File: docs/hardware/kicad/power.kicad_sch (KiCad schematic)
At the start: 18 parts, among them K1 125 A 24 V, Q1 IRLZ44N

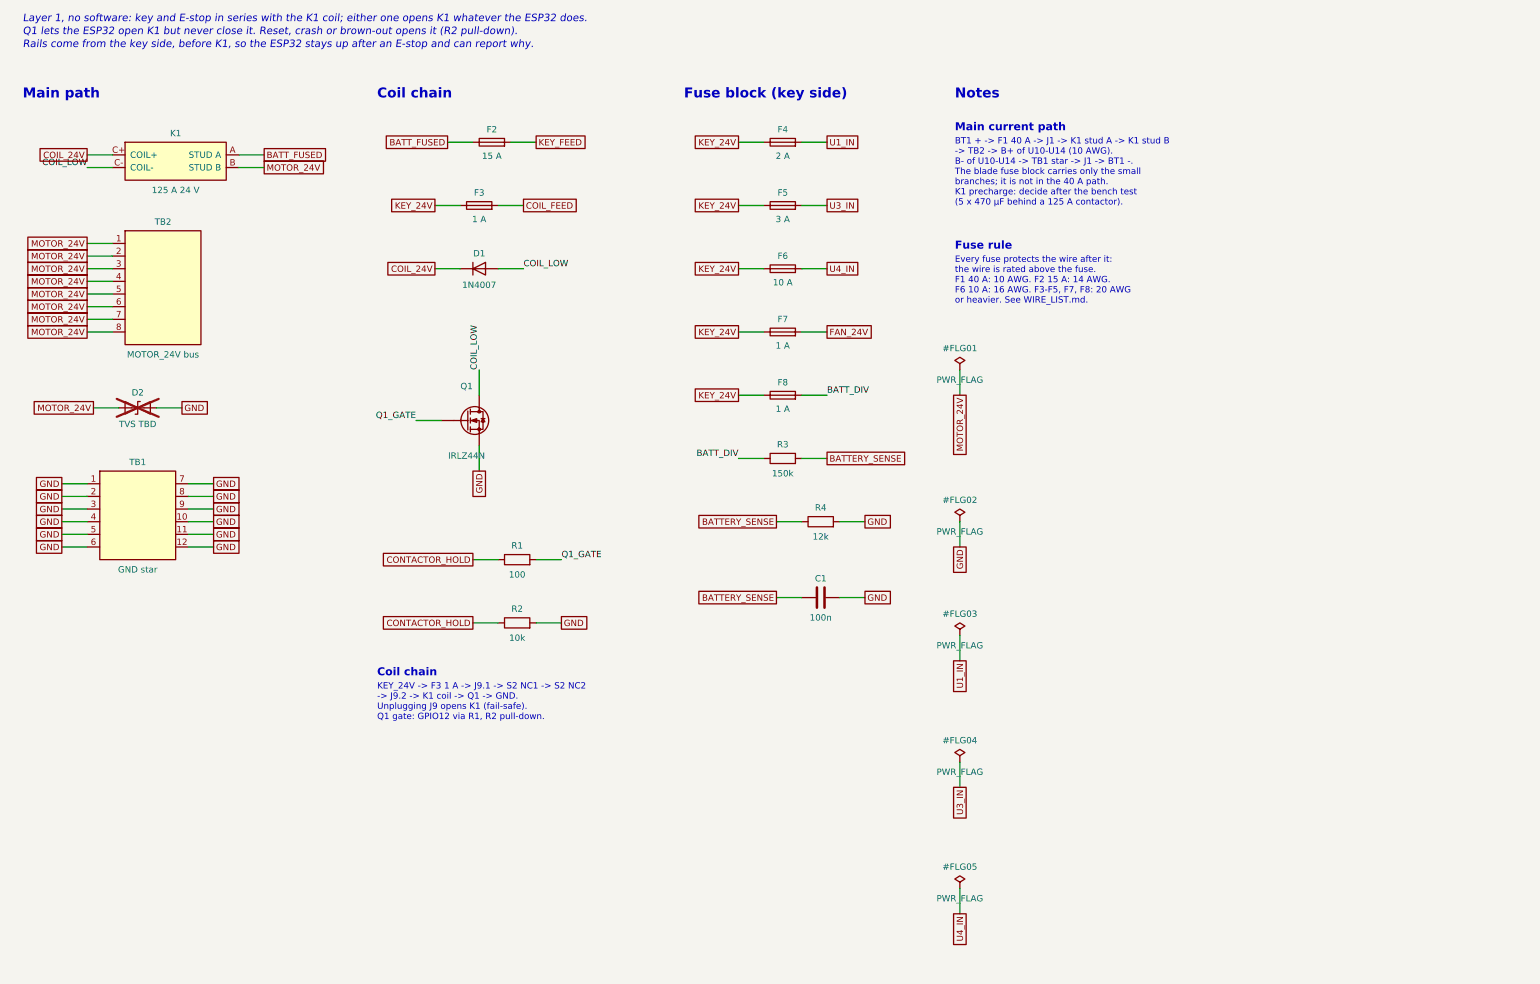
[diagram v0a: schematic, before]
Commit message: Match the firmware to schematic v0.3: current scaling, contactor checks, fans
- Current sense divides by half the per-pin IS resistor (IS_PIN_RESISTOR_OHMS),
  since R_IS and L_IS are joined; it read about half the real current before.
  The DRIVER level now comes from the resistor (1.8 V with 1k boards).
- DRIVER and OVERCUR open the contactor: a shorted MOSFET ignores DRIVE_EN.
  The drive enable drops before the contactor opens.
- Motor-bus sense: R5-R7 in the schematic (150k/12k to ADS1115 #2 A2, 2.2k
  bleed). New ContactorCheck: K1 stays open at boot until the bus drains
  (K1_WELD if it doesn't, permanent), and NO_BUS when K1 is held closed with
  no bus.
- I2C at 100 kHz, the PCF8574's rating.
- Box fans full on through PCA9685 channel 1; DS18B20 read with our own
  1-Wire timing; new HOT fault (65 C, hysteresis to 55 C).
- WHEEL_REVERSED per wheel in config.h.

Co-Authored-By: Claude Opus 5.5 (1M context) <noreply@anthropic.com>
Claude-Session: https://claude.ai/code/session_01BrgYX7MqpwRKNfNAgoiyH8
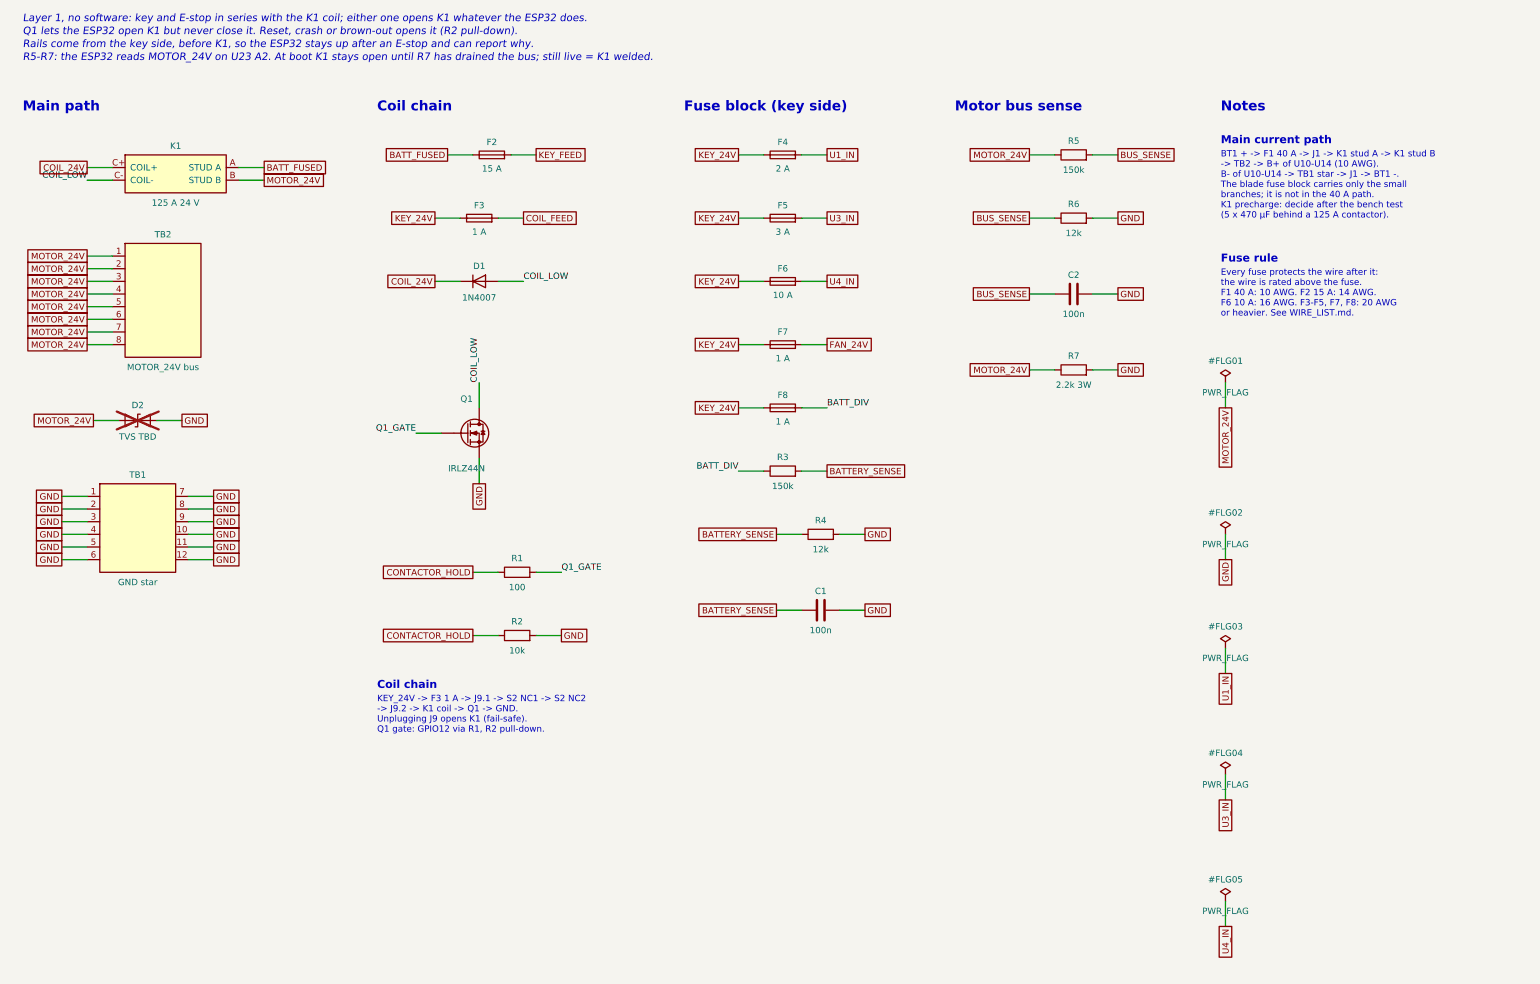
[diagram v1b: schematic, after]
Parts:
- added C2: 100n, symbol Device:C
- added R5: 150k, symbol Device:R
- added R6: 12k, symbol Device:R
- added R7: 2.2k 3W, symbol Device:R
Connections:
- net GND: now also C2.2, R6.2, R7.2
- net MOTOR_24V: now also R5.1, R7.1
- new net BUS_SENSE: C2.1, R5.2, R6.1
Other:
- note added: "Motor bus sense"
- note added: "R5-R7: the ESP32 reads MOTOR_24V on U23 A2. At boot K1 stays open until R7 has drained the bus; still live = K1 welded."
- moved on the sheet: C1, D1, D2, F2, F3, F4, F5, F6, F7, F8, K1, Q1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
